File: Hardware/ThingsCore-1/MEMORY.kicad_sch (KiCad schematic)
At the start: 2 parts, among them U8 W25Q256JVEIQ, U9 TF-PUSH

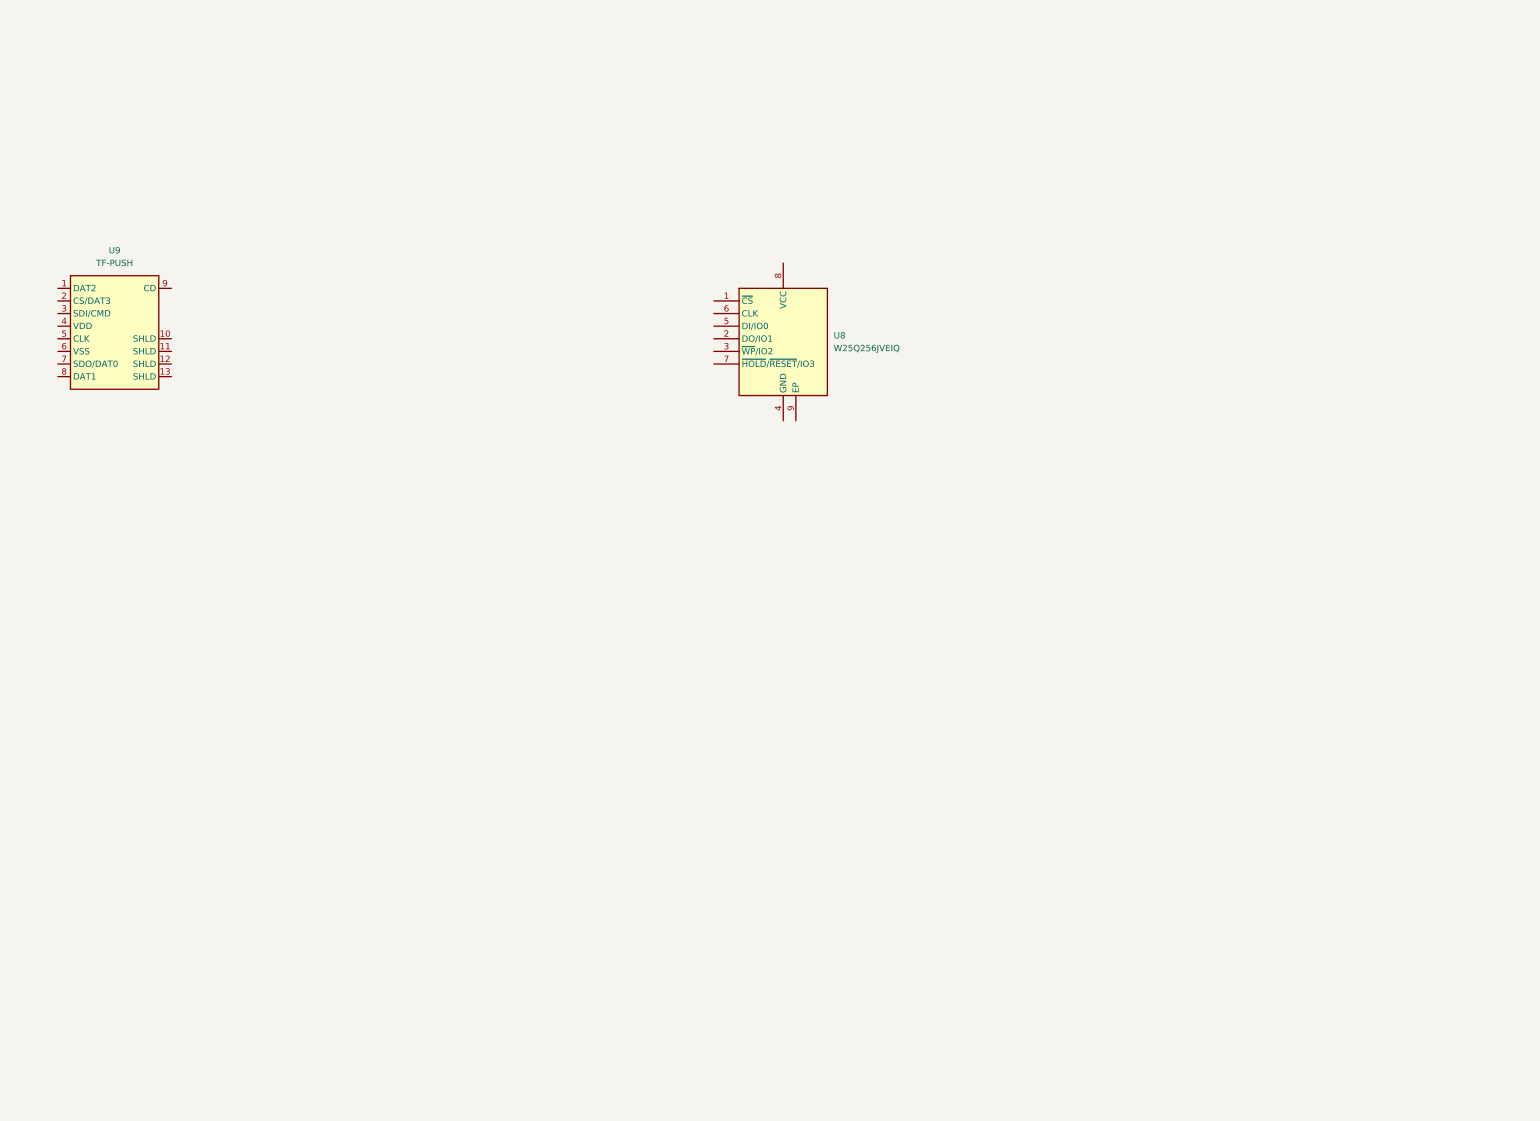
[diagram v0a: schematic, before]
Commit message: layout transciever components, pin selection and last components
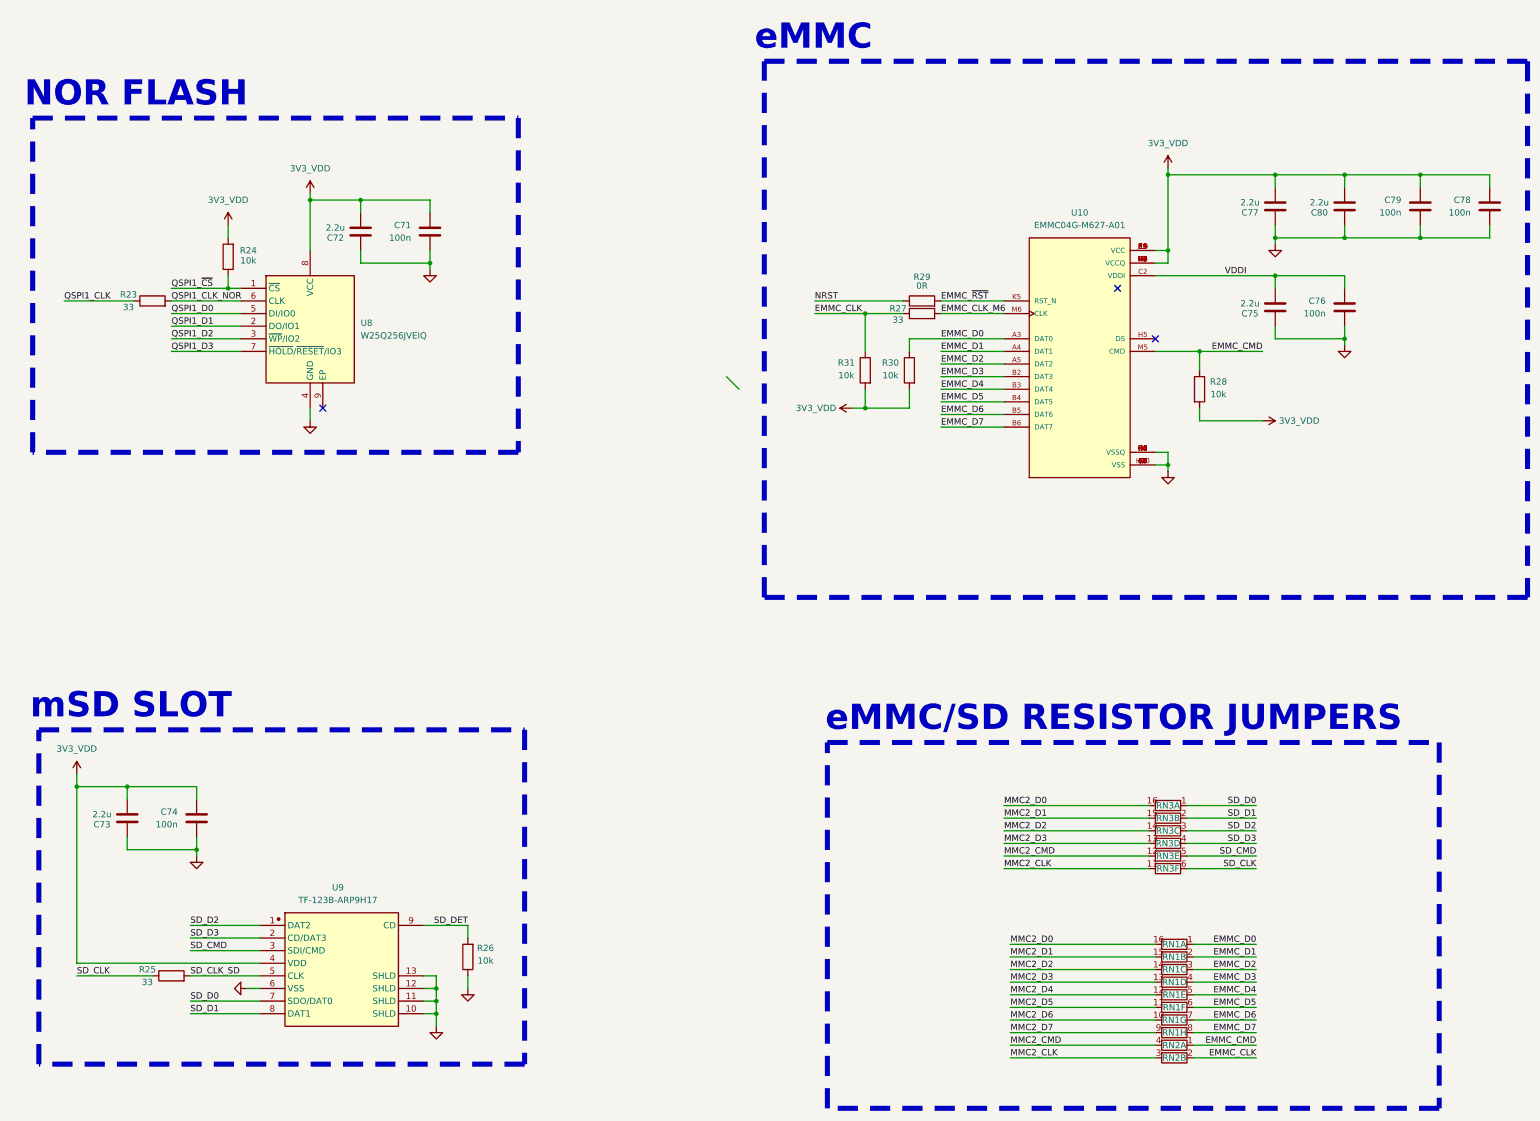
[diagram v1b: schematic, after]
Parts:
- removed U9: TF-PUSH, ThingsCore-1:TF-PUSH, symbol ThingsCore-1:TF-PUSH
- added C71, C74, C76, C78, C79: 100n, Capacitor_SMD:C_0402_1005Metric, symbol Device:C
- added C72, C73, C75, C77, C80: 2.2u, Capacitor_SMD:C_0402_1005Metric, symbol Device:C
- added R23, R25, R27: 33, Resistor_SMD:R_0402_1005Metric, symbol Device:R
- added R24, R26, R28, R30, R31: 10k, Resistor_SMD:R_0402_1005Metric, symbol Device:R
- added R29: 0R, Resistor_SMD:R_0402_1005Metric, symbol Device:R
- added RN1, RN3: R_Pack08_Split, ThingsCore-1:RESCAXS50P400X160X55-16N, symbol Device:R_Pack08_Split
- added RN2: R_Pack02_Split, Resistor_SMD:R_Array_Convex_2x0402, symbol Device:R_Pack02_Split
- added U10: EMMC04G-M627-A01, ThingsCore-1:BGA153C50P14X14_1300X1150X100, symbol ThingsCore-1:EMMC04G-M627-A01
- added U9: TF-123B-ARP9H17, ThingsCore-1:TF-SMD_TF-123-ARP9H15, symbol ThingsCore-1:TF-123B-ARP9H17
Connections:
- net QSPI1_~{CS}: now reaches U8.1 (~{CS})
- net QSPI1_~{CS}: now also R24.1
- net QSPI1_D1: now reaches U8.2 (DO/IO1)
- net QSPI1_D2: now reaches U8.3 (~{WP}/IO2)
- net GND: now reaches U8.4 (GND)
- net GND: now also C71.1, C72.2, C73.2, C74.1, C75.2, C76.1, C77.2, C78.1, C79.1, C80.2, R26.1, U10.A6 (VSS), U10.C4 (VSSQ), U10.E7 (VSS), U10.G5 (VSS), U10.H10 (VSS), U10.J5 (VSS), U10.K8 (VSS), U10.N2 (VSSQ), U10.N5 (VSSQ), U10.P4 (VSSQ), U10.P6 (VSSQ), U9.10 (SHLD), U9.11 (SHLD), U9.12 (SHLD), U9.13 (SHLD), U9.6 (VSS)
- net QSPI1_D0: now reaches U8.5 (DI/IO0)
- net QSPI1_CLK_NOR: now reaches U8.6 (CLK)
- net QSPI1_CLK_NOR: now also R23.2
- net QSPI1_D3: now reaches U8.7 (~{HOLD}/~{RESET}/IO3)
- net 3V3_VDD: now reaches U8.8 (VCC)
- net 3V3_VDD: now also C71.2, C72.1, C73.1, C74.2, C77.1, C78.2, C79.2, C80.1, R24.2, R28.2, R30.2, R31.2, U10.C6 (VCCQ), U10.E6 (VCC), U10.F5 (VCC), U10.J10 (VCC), U10.K9 (VCC), U10.M4 (VCCQ), U10.N4 (VCCQ), U10.P3 (VCCQ), U10.P5 (VCCQ), U9.4 (VDD)
- new net EMMC_CLK: R27.1, R31.1, RN2.2 (R2.1)
- new net EMMC_CLK_M6: R27.2, U10.M6 (CLK)
- new net EMMC_CMD: R28.1, RN2.1 (R1.1), U10.M5 (CMD)
- new net EMMC_D0: R30.1, RN1.1 (R1.1), U10.A3 (DAT0)
- new net EMMC_D1: RN1.2 (R2.1), U10.A4 (DAT1)
- new net EMMC_D2: RN1.3 (R3.1), U10.A5 (DAT2)
- new net EMMC_D3: RN1.4 (R4.1), U10.B2 (DAT3)
- new net EMMC_D4: RN1.5 (R5.1), U10.B3 (DAT4)
- new net EMMC_D5: RN1.6 (R6.1), U10.B4 (DAT5)
- new net EMMC_D6: RN1.7 (R7.1), U10.B5 (DAT6)
- new net EMMC_D7: RN1.8 (R8.1), U10.B6 (DAT7)
- new net EMMC_~{RST}: R29.2, U10.K5 (RST_N)
- new net MMC2_CLK: RN2.3 (R2.2), RN3.11 (R6.2)
- new net MMC2_CMD: RN2.4 (R1.2), RN3.12 (R5.2)
- new net MMC2_D0: RN1.16 (R1.2), RN3.16 (R1.2)
- new net MMC2_D1: RN1.15 (R2.2), RN3.15 (R2.2)
- new net MMC2_D2: RN1.14 (R3.2), RN3.14 (R3.2)
- new net MMC2_D3: RN1.13 (R4.2), RN3.13 (R4.2)
- new net MMC2_D4: RN1.12 (R5.2)
- new net MMC2_D5: RN1.11 (R6.2)
- new net MMC2_D6: RN1.10 (R7.2)
- new net MMC2_D7: RN1.9 (R8.2)
- new net NRST: R29.1
- new net QSPI1_CLK: R23.1
- new net SD_CLK: R25.1, RN3.6 (R6.1)
- new net SD_CLK_SD: R25.2, U9.5 (CLK)
- new net SD_CMD: RN3.5 (R5.1), U9.3 (SDI/CMD)
- new net SD_D0: RN3.1 (R1.1), U9.7 (SDO/DAT0)
- new net SD_D1: RN3.2 (R2.1), U9.8 (DAT1)
- new net SD_D2: RN3.3 (R3.1), U9.1 (DAT2)
- new net SD_D3: RN3.4 (R4.1), U9.2 (CD/DAT3)
- new net SD_DET: R26.2, U9.9 (CD)
- new net VDDI: C75.1, C76.2, U10.C2 (VDDI)
- no-connect marks 0 -> 3
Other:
- note added: "NOR FLASH"
- note added: "eMMC"
- note added: "eMMC/SD RESISTOR JUMPERS"
- note added: "mSD SLOT"
- moved on the sheet: U8

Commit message: pin assignment, rst,led, button pins left and checks
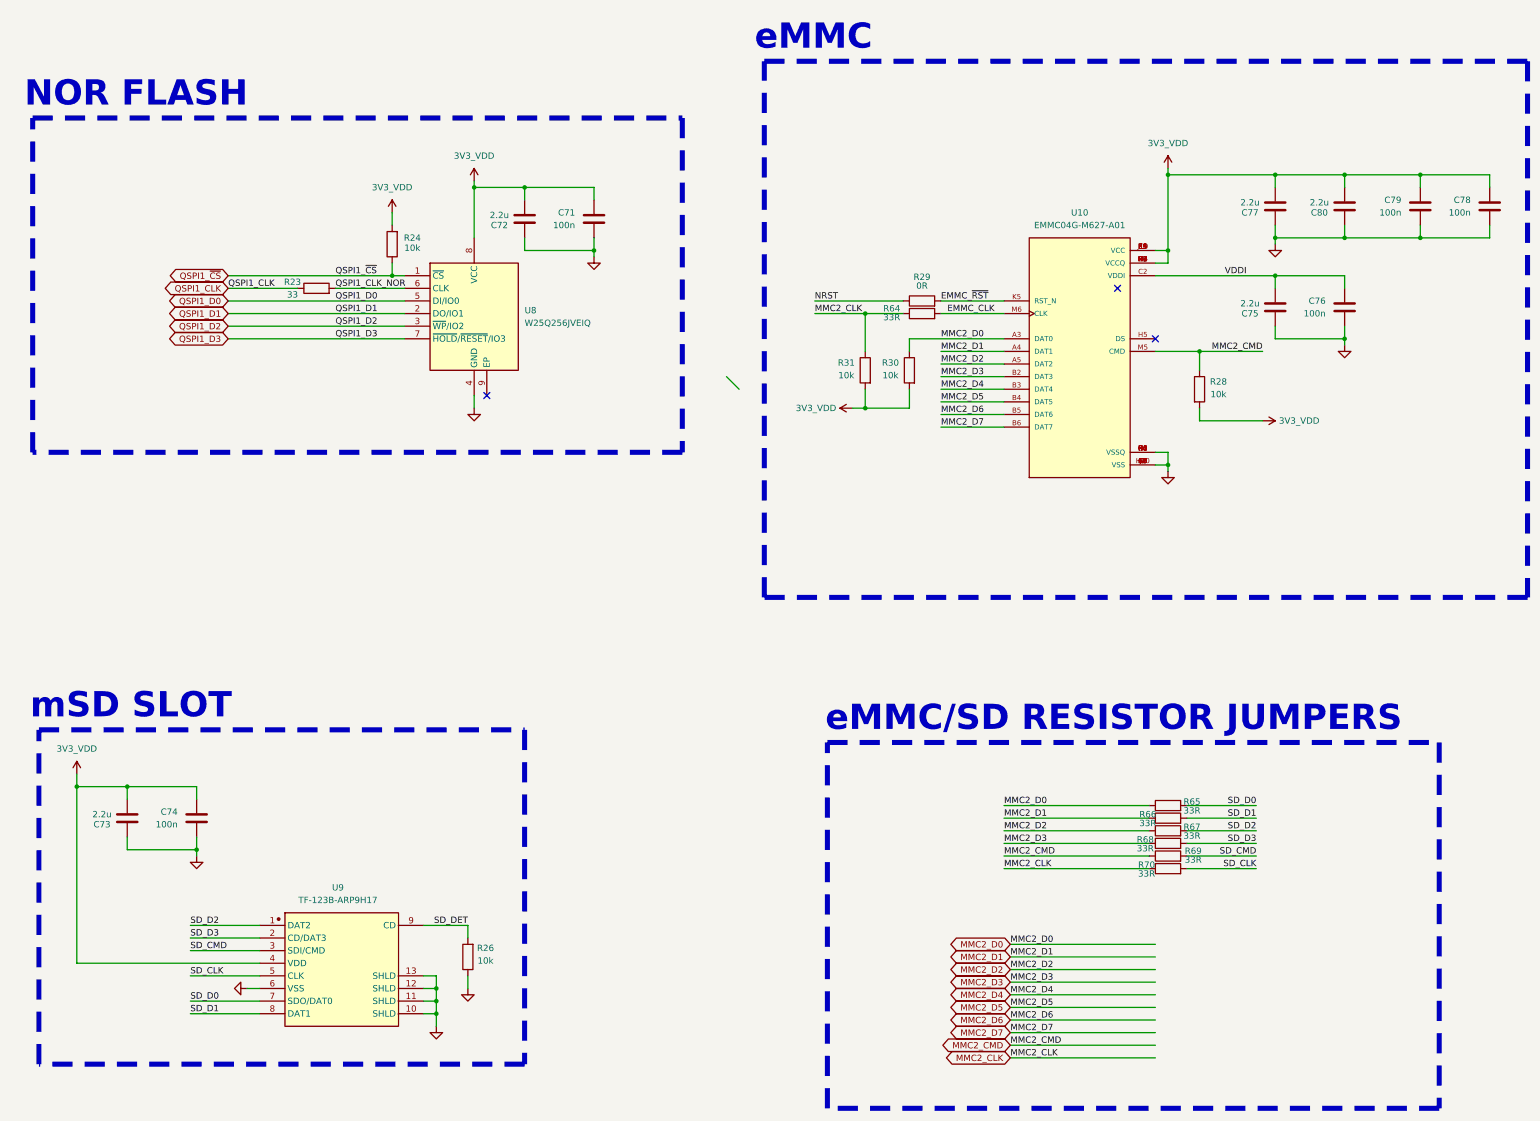
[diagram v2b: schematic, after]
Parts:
- removed R25, R27: 33, Resistor_SMD:R_0402_1005Metric, symbol Device:R
- removed RN1, RN3: R_Pack08_Split, ThingsCore-1:RESCAXS50P400X160X55-16N, symbol Device:R_Pack08_Split
- removed RN2: R_Pack02_Split, Resistor_SMD:R_Array_Convex_2x0402, symbol Device:R_Pack02_Split
- added R64, R65, R66, R67, R68, R69, R70: 33R, Resistor_SMD:R_0402_1005Metric, symbol Device:R
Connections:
- net EMMC_CLK_M6 is gone; now on net EMMC_CLK: U10.M6 (CLK)
- net EMMC_CMD is gone; now on net MMC2_CMD: R28.1, U10.M5 (CMD)
- net EMMC_D0 is gone; now on net MMC2_D0: R30.1, U10.A3 (DAT0)
- net EMMC_D1 is gone; now on net MMC2_D1: U10.A4 (DAT1)
- net EMMC_D2 is gone; now on net MMC2_D2: U10.A5 (DAT2)
- net EMMC_D3 is gone; now on net MMC2_D3: U10.B2 (DAT3)
- net EMMC_D4 is gone; now on net MMC2_D4: U10.B3 (DAT4)
- net EMMC_D5 is gone; now on net MMC2_D5: U10.B4 (DAT5)
- net EMMC_D6 is gone; now on net MMC2_D6: U10.B5 (DAT6)
- net EMMC_D7 is gone; now on net MMC2_D7: U10.B6 (DAT7)
- net SD_CLK_SD is gone; now on net SD_CLK: U9.5 (CLK)
- net EMMC_CLK: now also R64.2; no longer R31.1
- net MMC2_CLK: now also R31.1, R64.1, R70.1
- net MMC2_CMD: now also R69.1
- net MMC2_D0: now also R65.1
- net MMC2_D1: now also R66.1
- net MMC2_D2: now also R67.1
- net MMC2_D3: now also R68.1
- net SD_CLK: now also R70.2
- net SD_CMD: now also R69.2
- net SD_D0: now also R65.2
- net SD_D1: now also R66.2
- net SD_D2: now also R67.2
- net SD_D3: now also R68.2
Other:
- moved on the sheet: C71, C72, R23, R24, U8
